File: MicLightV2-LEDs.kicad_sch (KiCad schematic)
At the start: 56 parts, among them U10 NCR321UX, U11 NCR321UX, U4 NCR321UX, U5 NCR321UX, U6 NCR321UX, U7 NCR321UX, U8 NCR321UX, U9 NCR321UX

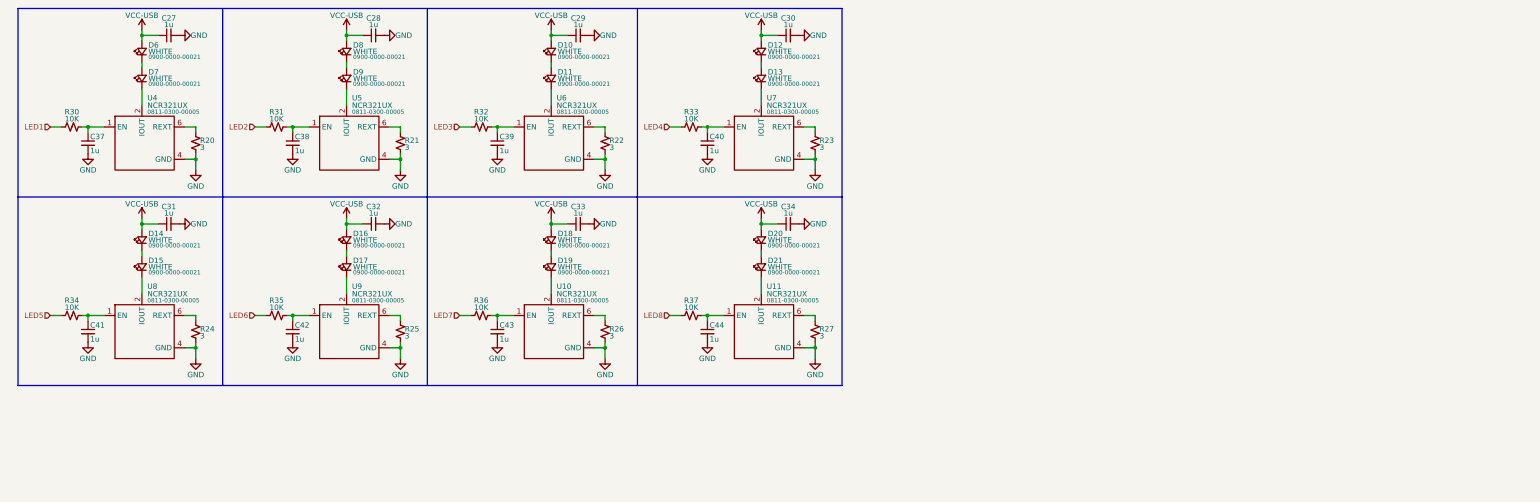
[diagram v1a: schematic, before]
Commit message: REV2 - add DAC and cc led drivers
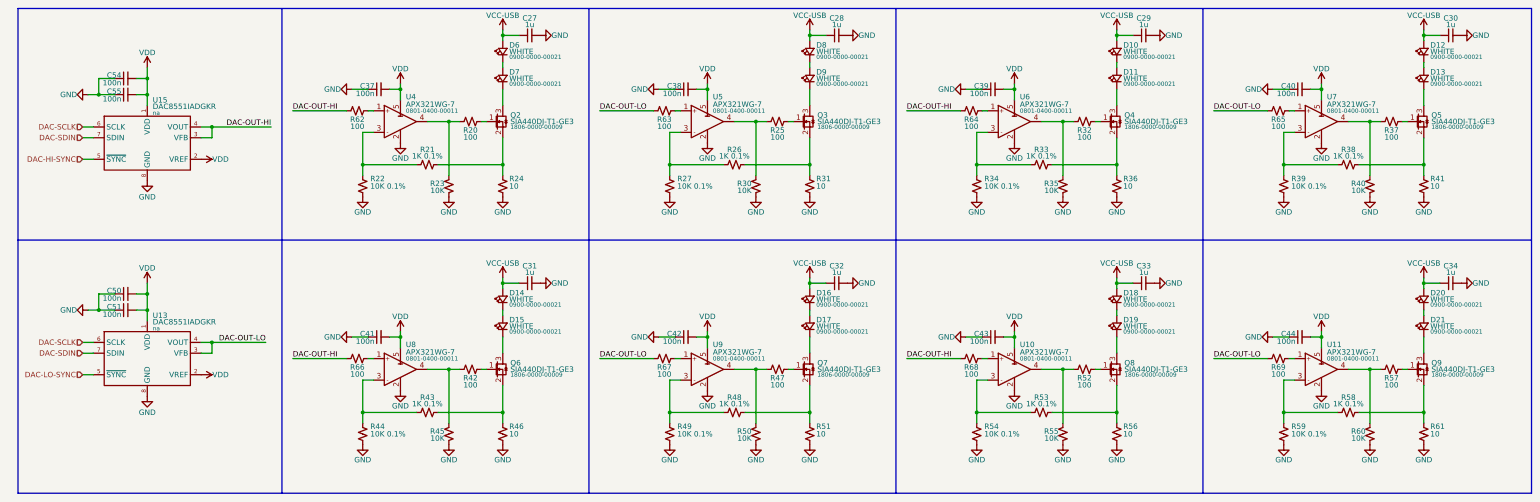
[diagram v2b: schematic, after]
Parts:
- removed C37, C38, C39, C40, C41, C42, C43, C44: 1u, Daxxn_Standard_Capacitors:CAP_0402, symbol DX_Capacitor_Ceramic:CL05A105KO5NNNC
- removed R21, R22, R23, R24, R26, R27: 3, Daxxn_Standard_Resistors:RES_0805, symbol DX_Device:R
- removed R31, R32, R33, R34, R36, R37: 10K, Daxxn_Standard_Resistors:RES_0402, symbol DX_Resistor:RC0402JR-0710KL
- removed U10, U11, U4, U5, U6, U7, U8, U9: NCR321UX, Daxxn_Packages:TSOT-23-6, symbol DX_IC_PMIC_LEDRegulator:NCR321UX
- added C37, C38, C39, C40, C41, C42, C43, C44, C50, C51, C54, C55: 100n, Daxxn_Standard_Capacitors:CAP_0402, symbol DX_Capacitor_Ceramic:CL05A104KA5NNNC
- added Q2, Q3, Q4, Q5, Q6, Q7, Q8, Q9: SIA440DJ-T1-GE3, Daxxn_Packages:PowerPak_SC-70-6, symbol DX_Transistor_MOSFET:SIA440DJ-T1-GE3
- added R21, R26, R33, R38, R43, R48, R53, R58: 1K 0.1%, Daxxn_Standard_Resistors:RES_0402, symbol DX_Resistor_Precision:RT0402BRE071KL
- added R22, R27, R34, R39, R44, R49, R54, R59: 10K 0.1%, Daxxn_Standard_Resistors:RES_0402, symbol DX_Resistor_Precision:TNPW040210K0BEED
- added R23, R40, R45, R50, R55, R60: 10K, Daxxn_Standard_Resistors:RES_0402, symbol DX_Resistor:RC0402JR-0710KL
- added R24, R31, R36, R41, R46, R51, R56, R61: 10, Daxxn_Standard_Resistors:RES_1218, symbol DX_Resistor_Sense:CRCW121810R0FKEKHP
- added R32, R37, R42, R47, R52, R57: 100, Daxxn_Standard_Resistors:RES_0402, symbol DX_Device:R
- added R62, R63, R64, R65, R66, R67, R68, R69: 100, Daxxn_Standard_Resistors:RES_0402, symbol DX_Resistor:RC0402JR-07100RL
- added U10, U11, U4, U5, U6, U7, U8, U9: APX321WG-7, Daxxn_Packages:SOT-23-5, symbol DX_IC_Amplifier_OPAMP:APX321WG-7
- added U13, U15: DAC8551IADGKR, Daxxn_Packages:VSSOP-8_3.0x3.0mm_P0.65mm, symbol DX_IC_Analog_DAC:DAC8551IADGKR
- R20, R25: value 3 -> 100; footprint Daxxn_Standard_Resistors:RES_0805 -> Daxxn_Standard_Resistors:RES_0402
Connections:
- net LED1 is gone; now on an unnamed net: R30.1
- net GND: now also R30.2, R35.2, C37.1, C38.1, C39.1, C40.1, C41.1, C42.1, C43.1, C44.1, C50.1, C51.1, C54.1, C55.1, R22.2, R23.2, R24.2, R27.2, R31.2, R34.2, R36.2, R39.2, R40.2, R41.2, R44.2, R45.2, R46.2, R49.2, R50.2, R51.2, R54.2, R55.2, R56.2, R59.2, R60.2, R61.2, U10.2 (V-), U11.2 (V-), U13.8 (GND), U15.8 (GND), U4.2 (V-), U5.2 (V-), U6.2 (V-), U7.2 (V-), U8.2 (V-), U9.2 (V-); no longer R20.2, R25.2
- net at D19.1 (K): now also Q8.3 (D)
- net at D21.1 (K): now also Q9.3 (D)
- net at D15.1 (K): now also Q6.3 (D)
- net at D9.1 (K): now also Q3.3 (D)
- net at D11.1 (K): now also Q4.3 (D)
- net at R25.1: now also U5.4 (OUT)
- net at R20.1: now also R23.1, U4.4 (OUT)
- net at D7.1 (K): now also Q2.3 (D)
- net at D17.1 (K): now also Q7.3 (D)
- net at D13.1 (K): now also Q5.3 (D)
- net LED6: no longer names the net of R35.1
- net LED6: now also R32.1, U6.4 (OUT)
- new net: Q5.1 (G), R37.2
- new net: Q5.2 (S), R38.2, R41.1
- new net: R64.2, U6.1 (IN+)
- new net: R38.1, R39.1, U7.3 (IN-)
- new net: R33.1, R34.1, U6.3 (IN-)
- new net: Q4.2 (S), R33.2, R36.1
- new net: R69.2, U11.1 (IN+)
- new net: R37.1, R40.1, U7.4 (OUT)
- new net: R53.1, R54.1, U10.3 (IN-)
- new net: Q2.1 (G), R20.2
- new net: R42.1, R45.1, U8.4 (OUT)
- new net: Q8.2 (S), R53.2, R56.1
- new net: R63.2, U5.1 (IN+)
- new net: Q3.2 (S), R26.2, R31.1
- new net: R67.2, U9.1 (IN+)
- new net: R48.1, R49.1, U9.3 (IN-)
- new net: R47.1, R50.1, U9.4 (OUT)
- new net: Q7.2 (S), R48.2, R51.1
- new net: Q6.2 (S), R43.2, R46.1
- new net: R57.1, R60.1, U11.4 (OUT)
- new net: Q9.1 (G), R57.2
- new net: Q6.1 (G), R42.2
- new net: R68.2, U10.1 (IN+)
- new net: Q4.1 (G), R32.2
- new net: Q2.2 (S), R21.2, R24.1
- new net: R58.1, R59.1, U11.3 (IN-)
- new net: Q3.1 (G), R25.2
- new net: Q9.2 (S), R58.2, R61.1
- new net: Q8.1 (G), R52.2
- new net: R62.2, U4.1 (IN+)
- new net: R65.2, U7.1 (IN+)
- new net: R66.2, U8.1 (IN+)
- new net: R43.1, R44.1, U8.3 (IN-)
- new net: R52.1, R55.1, U10.4 (OUT)
- new net: R26.1, R27.1, U5.3 (IN-)
- new net: Q7.1 (G), R47.2
- new net: R21.1, R22.1, U4.3 (IN-)
- new net DAC-HI-SYNC: U15.5 (~{SYNC})
- new net DAC-LO-SYNC: U13.5 (~{SYNC})
- new net DAC-OUT-HI: R62.1, R64.1, R66.1, R68.1, U15.3 (VFB), U15.4 (VOUT)
- new net DAC-OUT-LO: R63.1, R65.1, R67.1, R69.1, U13.3 (VFB), U13.4 (VOUT)
- new net DAC-SCLK: U13.6 (SCLK), U15.6 (SCLK)
- new net DAC-SDIN: U13.7 (SDIN), U15.7 (SDIN)
- new net VDD: C37.2, C38.2, C39.2, C40.2, C41.2, C42.2, C43.2, C44.2, C50.2, C51.2, C54.2, C55.2, U10.5 (V+), U11.5 (V+), U13.1 (VDD), U13.2 (VREF), U15.1 (VDD), U15.2 (VREF), U4.5 (V+), U5.5 (V+), U6.5 (V+), U7.5 (V+), U8.5 (V+), U9.5 (V+)
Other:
- moved on the sheet: C27, C28, C29, C30, C31, C32, C33, C34, D10, D11, D12, D13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
